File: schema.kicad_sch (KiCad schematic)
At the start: 7 parts, among them U1 74HC595D, U2 74HC595D, U5 AT28C256-15PU

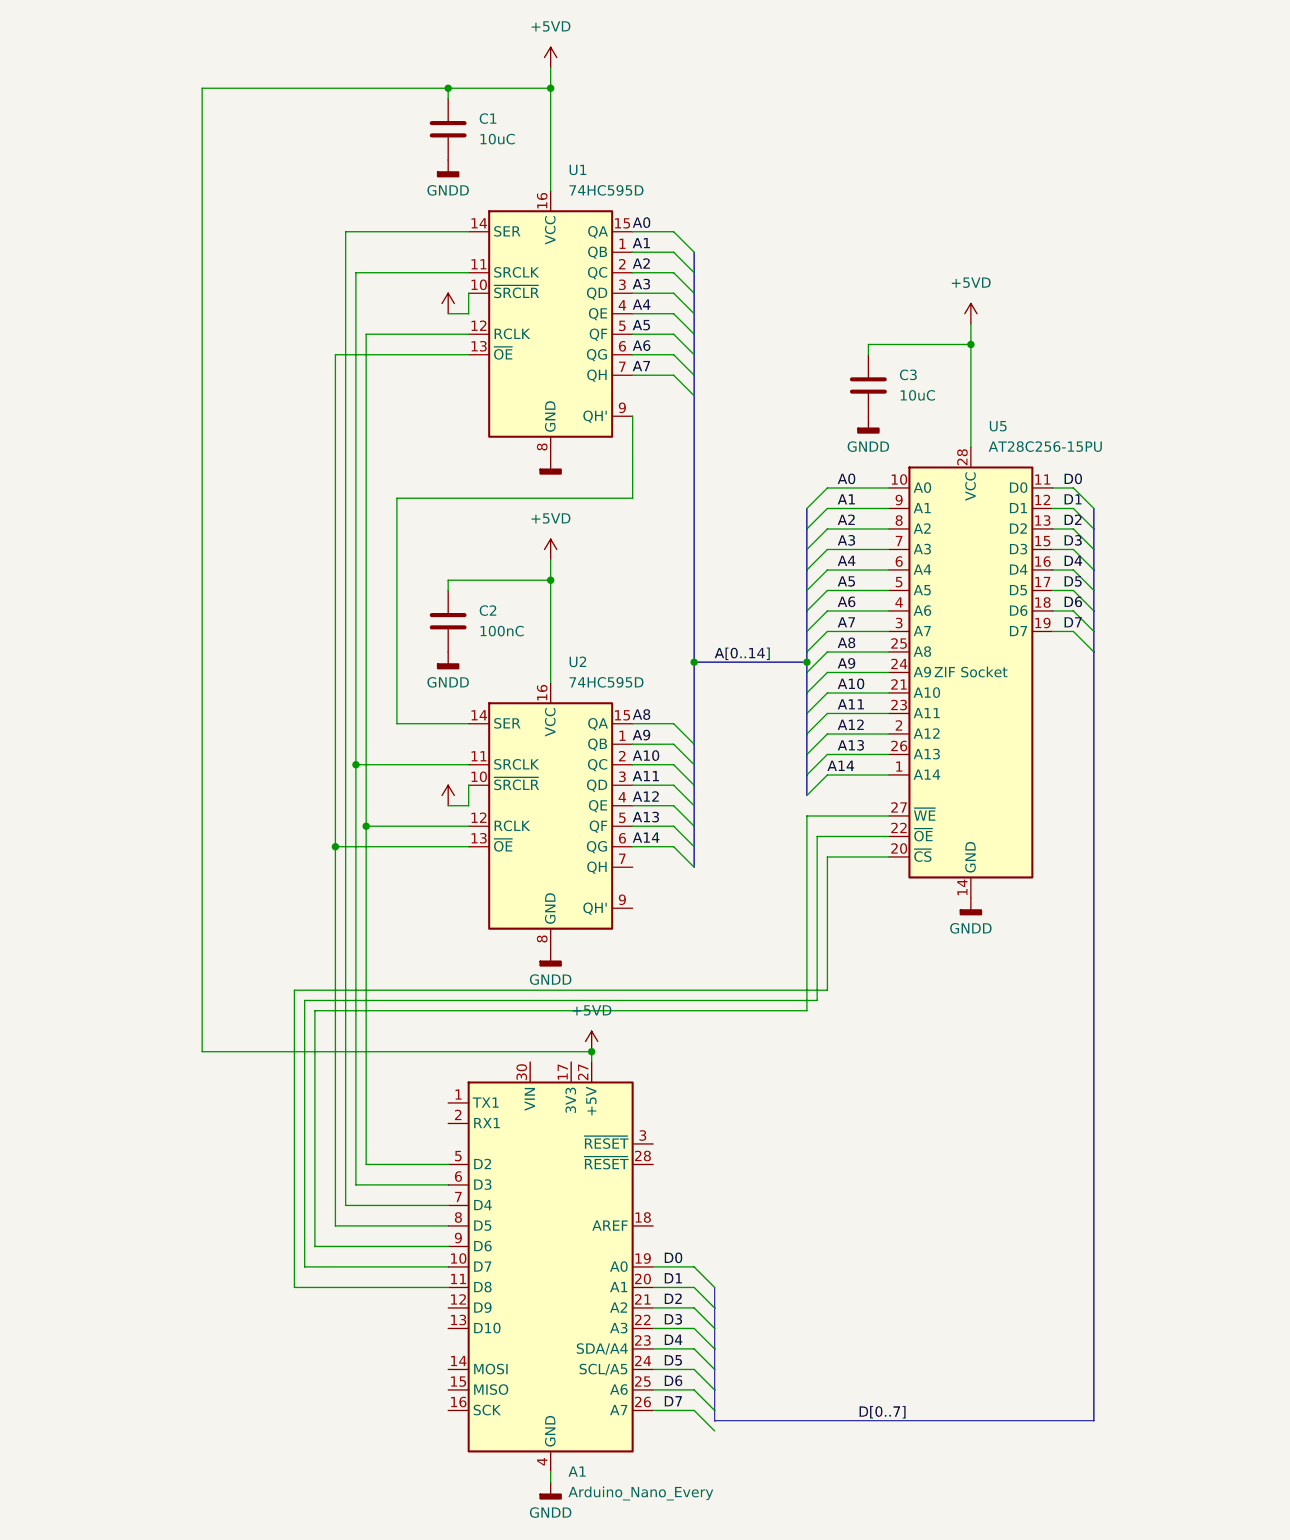
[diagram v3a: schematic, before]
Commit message: fix not enough digital pins
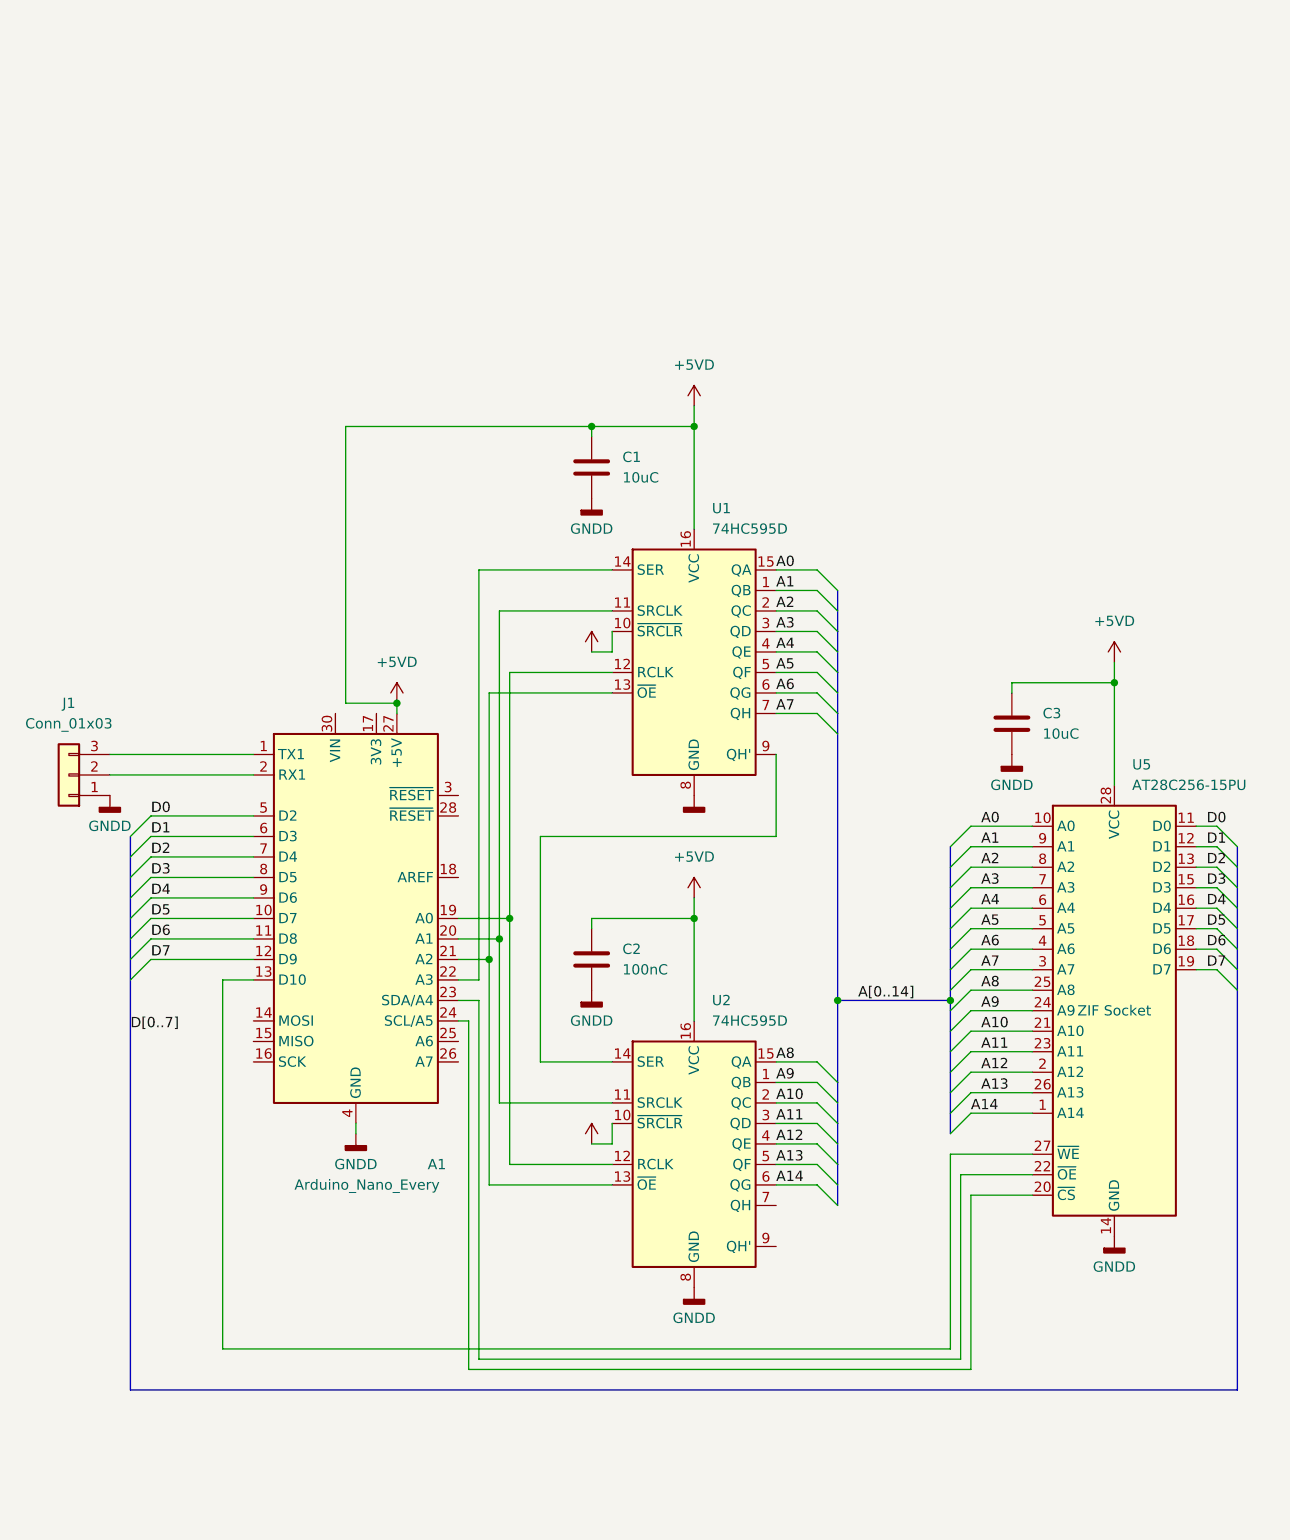
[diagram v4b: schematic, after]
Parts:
- added J1: Conn_01x03, Connector_PinHeader_2.54mm:PinHeader_1x03_P2.54mm_Vertical, symbol Connector_Generic:Conn_01x03
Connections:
- net D0: now also A1.5 (D2); no longer A1.19 (A0)
- net D1: now also A1.6 (D3); no longer A1.20 (A1)
- net D2: now also A1.7 (D4); no longer A1.21 (A2)
- net D3: now also A1.8 (D5); no longer A1.22 (A3)
- net D4: now also A1.9 (D6); no longer A1.23 (SDA/A4)
- net D5: now also A1.10 (D7); no longer A1.24 (SCL/A5)
- net D6: now also A1.11 (D8); no longer A1.25 (A6)
- net D7: now also A1.12 (D9); no longer A1.26 (A7)
- net GNDD: now also J1.1 (Pin_1)
- net at A1.1 (TX1): now also J1.3 (Pin_3)
- net at U5.22 (~{OE}): now also A1.23 (SDA/A4); no longer A1.10 (D7)
- net at U5.20 (~{CS}): now also A1.24 (SCL/A5); no longer A1.11 (D8)
- net at A1.13 (D10): now also U5.27 (~{WE})
- net at A1.2 (RX1): now also J1.2 (Pin_2)
- net at U1.12 (RCLK), U2.12 (RCLK): now also A1.19 (A0); no longer A1.5 (D2)
- net at U1.11 (SRCLK), U2.11 (SRCLK): now also A1.20 (A1); no longer A1.6 (D3)
- net at U1.14 (SER): now also A1.22 (A3); no longer A1.7 (D4)
- net at U1.13 (~{OE}), U2.13 (~{OE}): now also A1.21 (A2); no longer A1.8 (D5)
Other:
- moved on the sheet: A1, C1, C2, C3, U1, U2, U5
